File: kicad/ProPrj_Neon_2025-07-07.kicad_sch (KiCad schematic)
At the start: 14 parts, among them U2 NE555-TD, U5 47uH

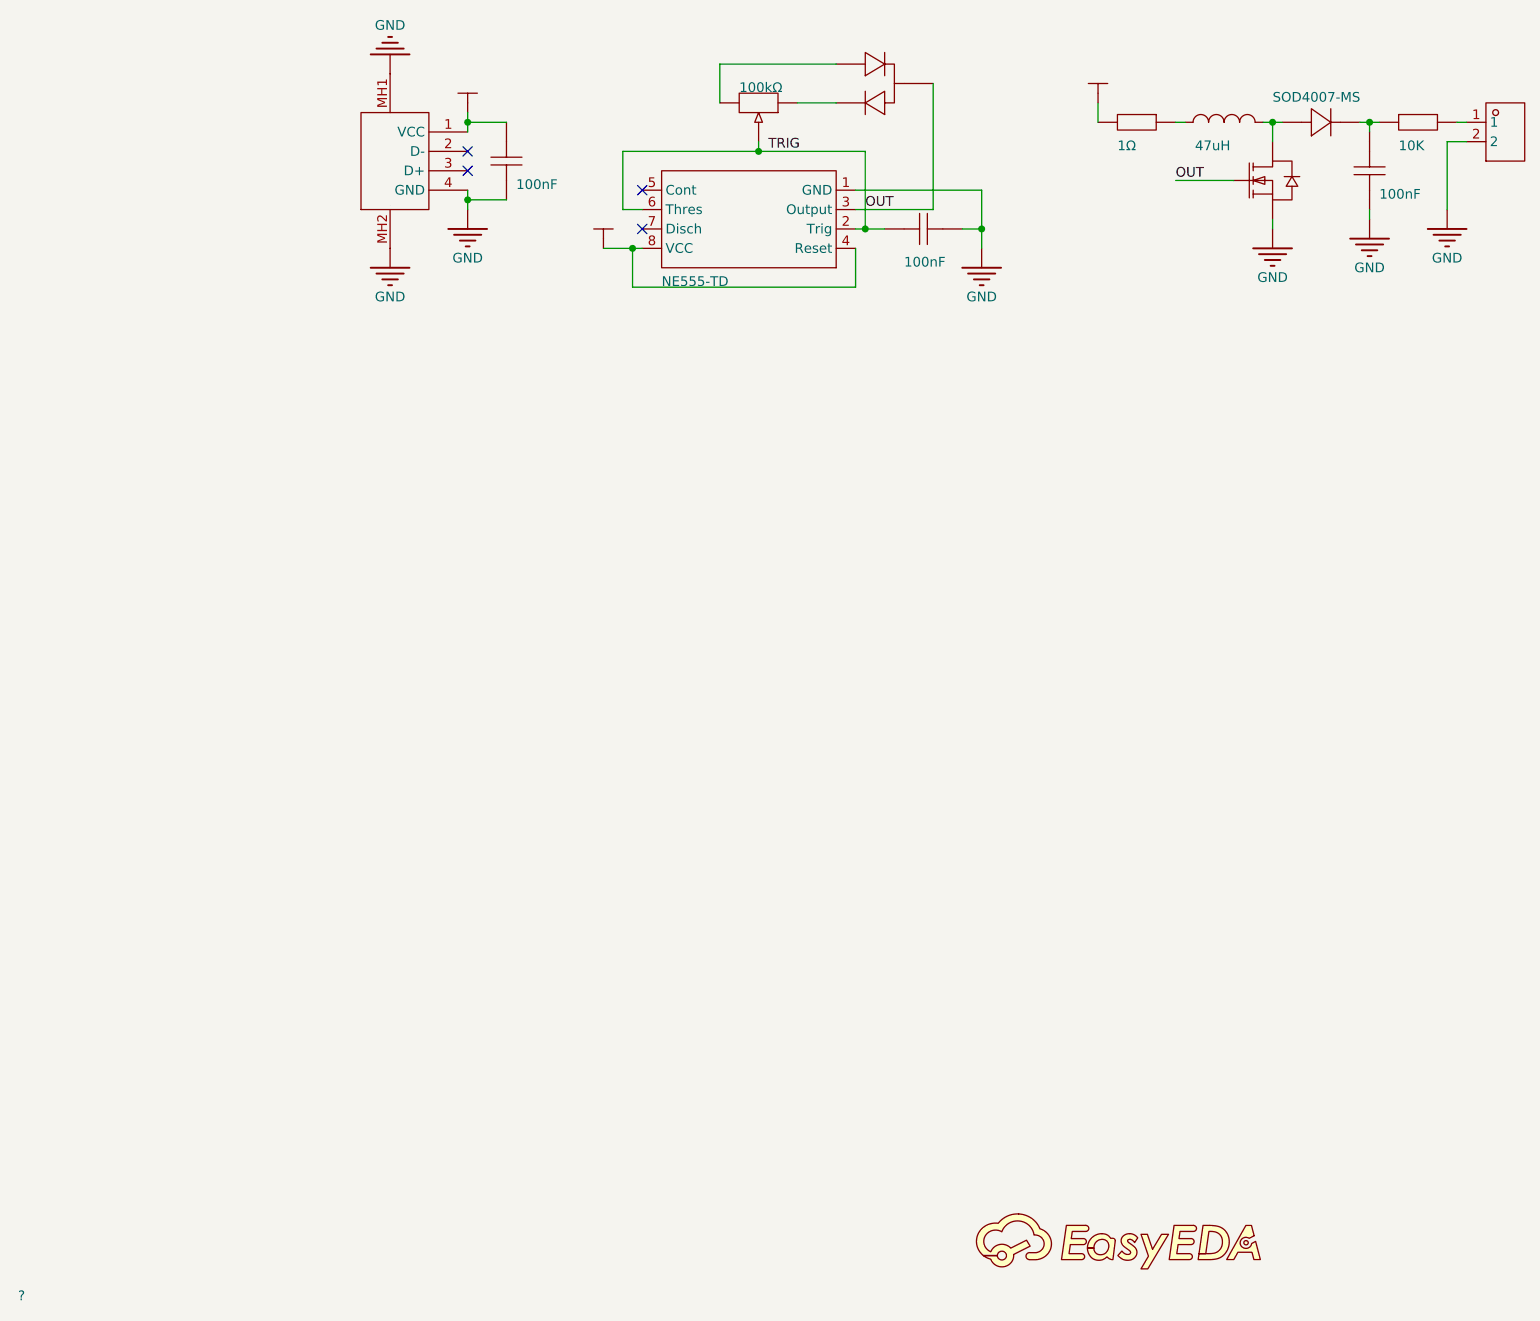
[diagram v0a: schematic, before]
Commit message: fix pcb import, html bom
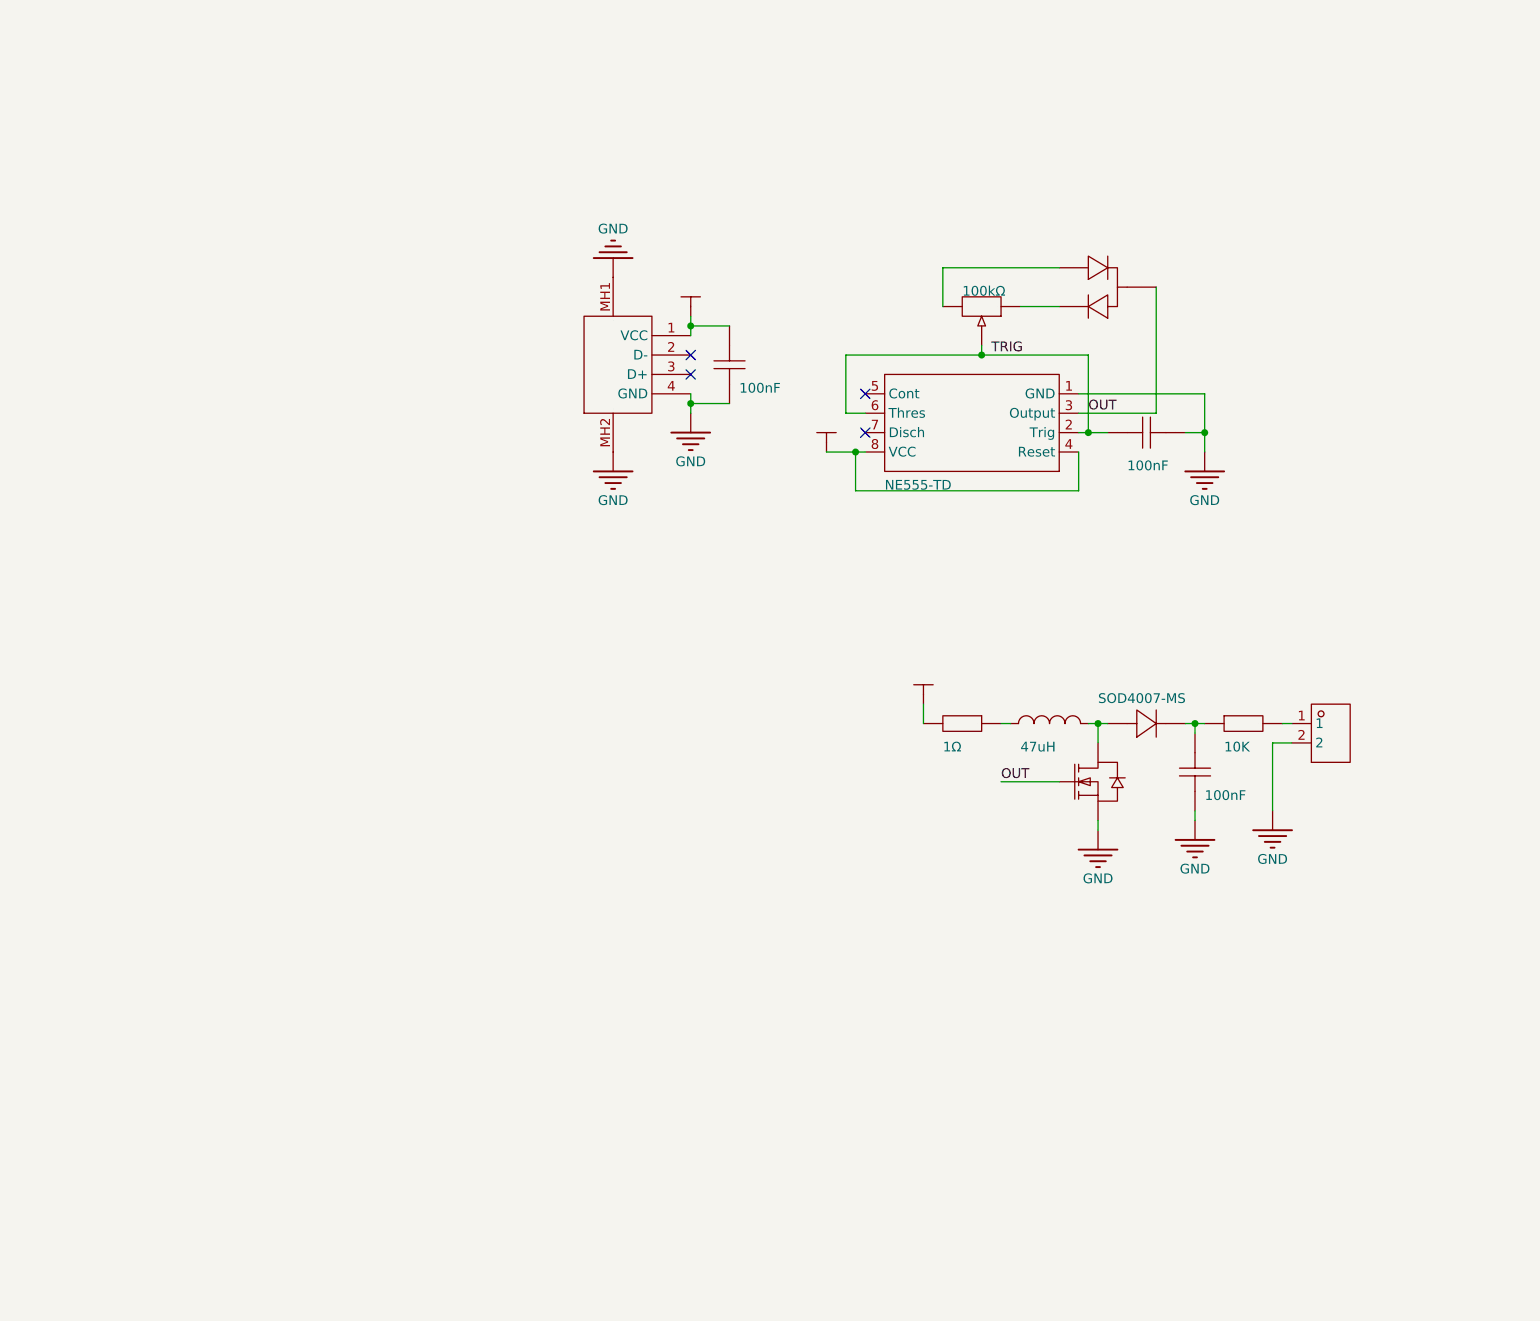
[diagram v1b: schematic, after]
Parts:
- removed ?: (no value), ProPrj_Neo-easyedapro:, symbol ProPrj_Neo-easyedapro:Drawing-Symbol_A4
- Q1, U3, U4, USB1: value (none) -> ~

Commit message: fix pcb symbols
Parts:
- C1, C2, C3: footprint ProPrj_Neo-easyedapro:C0603 -> ProPrj_Neon_2025-07-07:C0603
- D2: footprint ProPrj_Neo-easyedapro:SOD-123FL_L2.8-W1.8-LS3.7-RD -> ProPrj_Neon_2025-07-07:SOD-123FL_L2.8-W1.8-LS3.7-RD
- Q1: value ~ -> BSS123; footprint ProPrj_Neo-easyedapro:SOT-323-3_L2.0-W1.3-P1.30-LS2.3-BR -> ProPrj_Neon_2025-07-07:SOT-323-3_L2.0-W1.3-P1.30-LS2.3-BR
- R3, R5: footprint ProPrj_Neo-easyedapro:R0603 -> ProPrj_Neon_2025-07-07:R0603
- R4: footprint ProPrj_Neo-easyedapro:RES-ADJ-TH_3P-L9.5-W4.9-P2.50-L_3296W -> ProPrj_Neon_2025-07-07:RES-ADJ-TH_3P-L9.5-W4.9-P2.50-L_3296W
- U2: footprint ProPrj_Neo-easyedapro:SOIC-8_L4.9-W3.9-P1.27-LS6.0-BL -> ProPrj_Neon_2025-07-07:SOIC-8_L4.9-W3.9-P1.27-LS6.0-BL
- U3: footprint ProPrj_Neo-easyedapro:HDR-TH_2P-P2.54-H-F-W10.0-N -> ProPrj_Neon_2025-07-07:HDR-TH_2P-P2.54-H-F-W10.0-N
- U4: value ~ -> BAV99; footprint ProPrj_Neo-easyedapro:SOT-23-3_L3.0-W1.7-P0.95-LS2.9-BR -> ProPrj_Neon_2025-07-07:SOT-23-3_L3.0-W1.7-P0.95-LS2.9-BR
- U5: footprint ProPrj_Neo-easyedapro:IND-TH_BD4.0-L10.5-P14.50-D0.6 -> ProPrj_Neon_2025-07-07:IND-TH_BD3.2-L7.0-P11.00-D0.5
- USB1: footprint ProPrj_Neo-easyedapro:USB-AM-TH_AM90 -> ProPrj_Neon_2025-07-07:USB-AM-TH_AM90
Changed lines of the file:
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@@
 			)
 		)
-		(property "Footprint" "ProPrj_Neo-easyedapro:HDR-TH_2P-P2.54-H-F-W10.0-N"
+		(property "Footprint" "ProPrj_Neon_2025-07-07:HDR-TH_2P-P2.54-H-F-W10.0-N"
 			(at 127 91.44 0)
 			(effects
@@
 			)
 		)
-		(property "Footprint" "ProPrj_Neo-easyedapro:USB-AM-TH_AM90"
+		(property "Footprint" "ProPrj_Neon_2025-07-07:USB-AM-TH_AM90"
 			(at 33.02 44.45 0)
 			(effects
@@
 			)
 		)
-		(property "Value" "~"
-			(at 97.79 33.02 0)
-			(effects
-				(font
-					(size 1.27 1.27)
-				)
-			)
-		)
-		(property "Footprint" "ProPrj_Neo-easyedapro:SOT-23-3_L3.0-W1.7-P0.95-LS2.9-BR"
+		(property "Value" "BAV99"
+			(at 102.616 31.496 90)
+			(effects
+				(font
+					(size 1.27 1.27)
+				)
+			)
+		)
+		(property "Footprint" "ProPrj_Neon_2025-07-07:SOT-23-3_L3.0-W1.7-P0.95-LS2.9-BR"
 			(at 97.79 33.02 0)
 			(effects
@@
 			)
 		)
-		(property "Footprint" "ProPrj_Neo-easyedapro:IND-TH_BD4.0-L10.5-P14.50-D0.6"
+		(property "Footprint" "ProPrj_Neon_2025-07-07:IND-TH_BD3.2-L7.0-P11.00-D0.5"
 			(at 90.17 90.17 0)
 			(effects
@@
 			)
 		)
-		(property "Footprint" "ProPrj_Neo-easyedapro:R0603"
+		(property "Footprint" "ProPrj_Neon_2025-07-07:R0603"
 			(at 115.57 90.17 0)
 			(effects
@@
 			)
 		)
-		(property "Value" "~"
-			(at 96.52 95.25 0)
-			(effects
-				(font
-					(size 1.27 1.27)
-				)
-			)
-		)
-		(property "Footprint" "ProPrj_Neo-easyedapro:SOT-323-3_L2.0-W1.3-P1.30-LS2.3-BR"
+		(property "Value" "BSS123"
+			(at 101.092 93.98 0)
+			(effects
+				(font
+					(size 1.27 1.27)
+				)
+			)
+		)
+		(property "Footprint" "ProPrj_Neon_2025-07-07:SOT-323-3_L2.0-W1.3-P1.30-LS2.3-BR"
 			(at 96.52 95.25 0)
 			(effects
@@
 			)
 		)
-		(property "Footprint" "ProPrj_Neo-easyedapro:R0603"
+		(property "Footprint" "ProPrj_Neon_2025-07-07:R0603"
 			(at 78.74 90.17 0)
 			(effects
@@
 			)
 		)
-		(property "Footprint" "ProPrj_Neo-easyedapro:C0603"
+		(property "Footprint" "ProPrj_Neon_2025-07-07:C0603"
 			(at 102.87 52.07 0)
 			(effects
@@
 			)
 		)
-		(property "Footprint" "ProPrj_Neo-easyedapro:SOIC-8_L4.9-W3.9-P1.27-LS6.0-BL"
+		(property "Footprint" "ProPrj_Neon_2025-07-07:SOIC-8_L4.9-W3.9-P1.27-LS6.0-BL"
 			(at 80.01 50.8 0)
 			(effects
@@
 			)
 		)
-		(property "Footprint" "ProPrj_Neo-easyedapro:C0603"
+		(property "Footprint" "ProPrj_Neon_2025-07-07:C0603"
 			(at 48.26 43.18 0)
 			(effects
@@
 			)
 		)
-		(property "Footprint" "ProPrj_Neo-easyedapro:C0603"
+		(property "Footprint" "ProPrj_Neon_2025-07-07:C0603"
 			(at 109.22 96.52 0)
 			(effects
@@
 			)
 		)
-		(property "Footprint" "ProPrj_Neo-easyedapro:SOD-123FL_L2.8-W1.8-LS3.7-RD"
+		(property "Footprint" "ProPrj_Neon_2025-07-07:SOD-123FL_L2.8-W1.8-LS3.7-RD"
 			(at 102.87 90.17 0)
 			(effects
@@
 		)
 		(property "Value" "100kΩ"
-			(at 78.74 34.29 90)
+			(at 78.74 33.782 90)
 			(effects
 				(font
@@
 			)
 		)
-		(property "Footprint" "ProPrj_Neo-easyedapro:RES-ADJ-TH_3P-L9.5-W4.9-P2.50-L_3296W"
+		(property "Footprint" "ProPrj_Neon_2025-07-07:RES-ADJ-TH_3P-L9.5-W4.9-P2.50-L_3296W"
 			(at 81.28 35.56 0)
 			(effects
